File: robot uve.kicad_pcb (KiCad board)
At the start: 2 copper layers, 100 x 100 mm, 63 parts, among them J1 pulsador1, J10 HC-SR04, J11 HC-SR04, J12 HC-SR04, J13 NC - C - NA, J14 I2C_B, J15 I2C_C, J16 NeoPixel, J17 neopixel, J18 +5V IN, J19 GND, J2 I2C_A, J20 pulsador2, J21 IR, J22 pulsador2, J3 NC - C - NA, J4 comunicacion a rpi, J5 12V IN, J6 GND, J7 HC-SR04, J8 HC-SR04, J9 HC-SR04, K1 RELAY_C, K3 RELAY_C, P1 Digital, P10 CONN_01X01, P11 CONN_01X01, P12 CONN_01X01, P13 CONN_01X01, P14 motor3, P15 motor2, P16 Sensores de Linea, P17 motor1, P18 motor4, P2 Power, P3 Analog, P4 Analog, P5 PWM, P6 PWM, P7 Communication, P8 CONN_01X01, P9 CONN_01X01, Q1 2N7002, Q3 2N7002, Q4 2N7002, SW1 RST

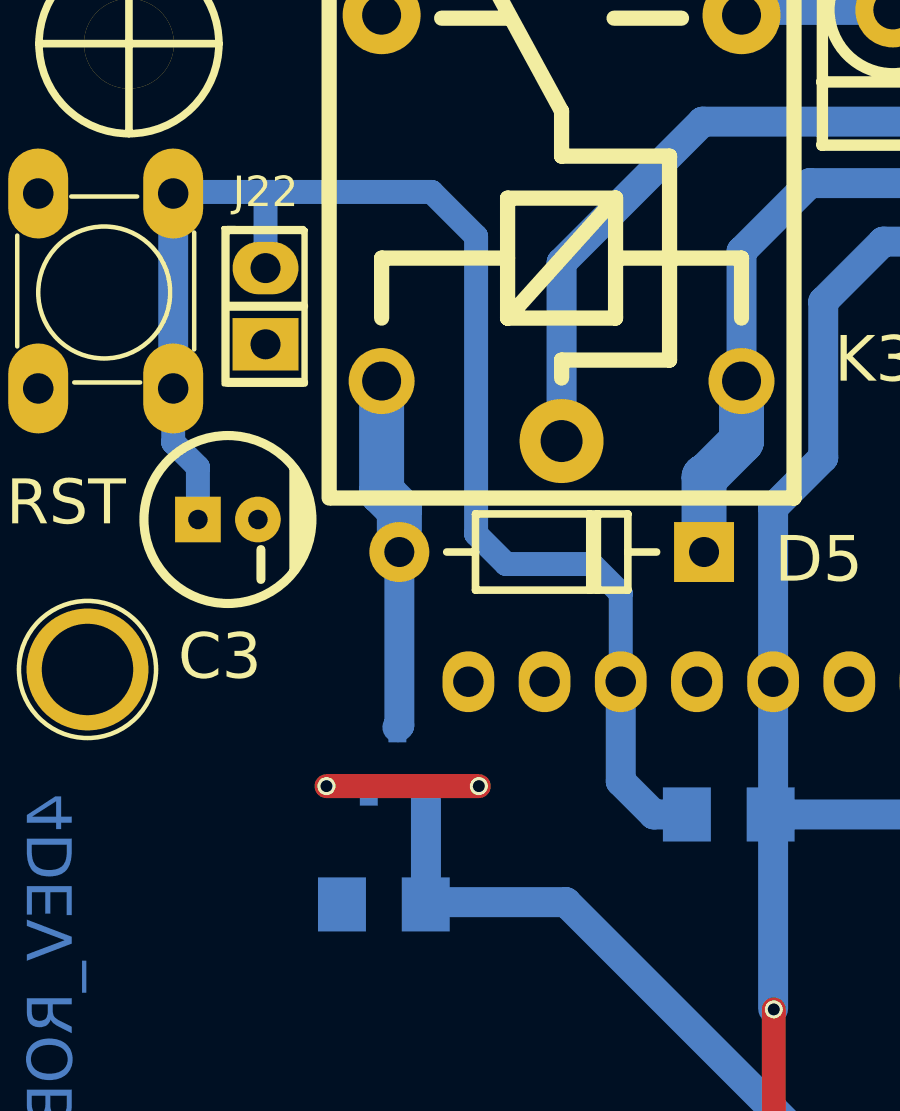
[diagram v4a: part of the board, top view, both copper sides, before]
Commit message: Img Pinout + avances en pcb
Agregue la imagen del pinout del arduino Mega en el sch, esta en una escala muy baja para que no moleste, en caso de necesitar revisar algo, cambiar la escala y luego volverla a la actual.
Cambie el icono del rotulo de SCH.
Movi un SOT-23 para que el poligono de GND pueda pasar por debajo del relay y evitar un jumper.
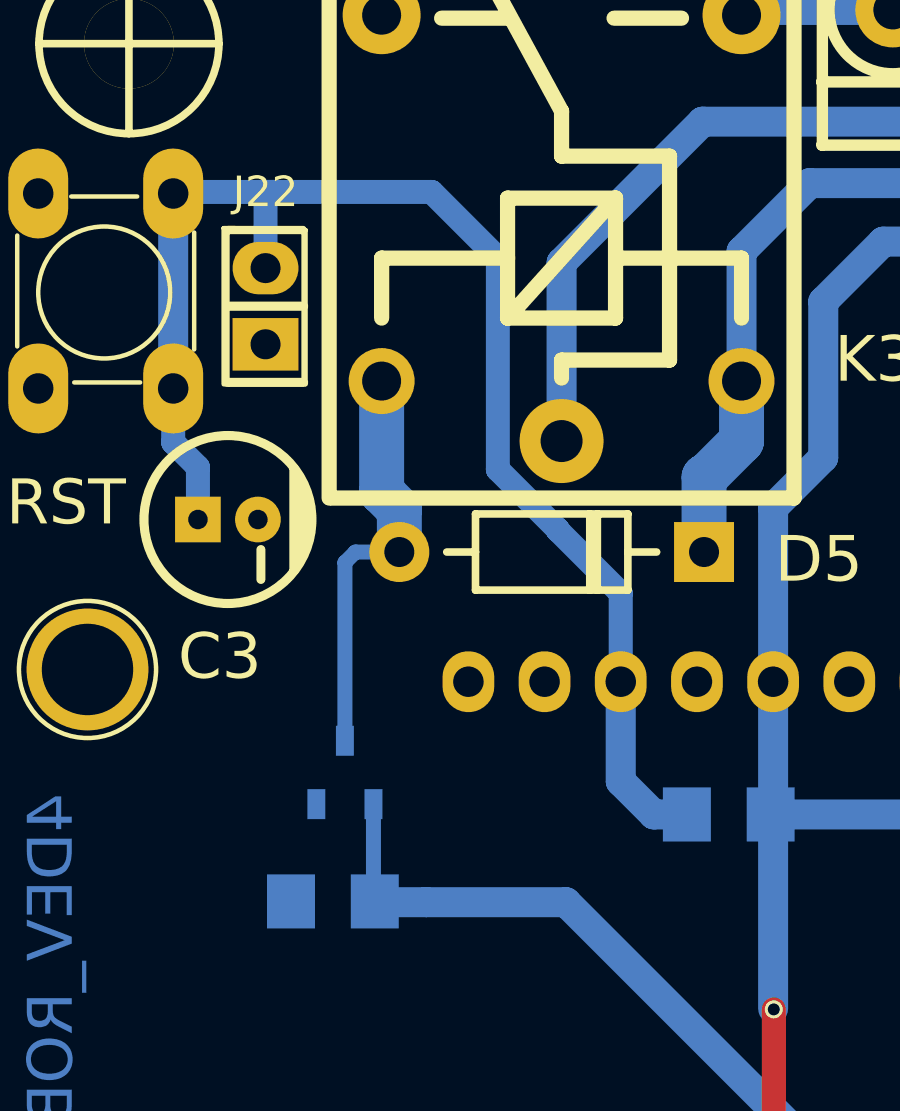
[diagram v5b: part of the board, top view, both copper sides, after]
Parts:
- moved Q4 1.81 mm to (117.2, 79.3)
- moved R5 1.70 mm to (116.8, 83.6)
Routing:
- net GND: track 64.3 -> 59.2 mm, vias 26 -> 24
- net Net-(D5-Pad1): track 11.8 -> 13.8 mm
- net /Reset: track 49.9 -> 48.2 mm
- net /3(**): track 59.5 -> 60.8 mm

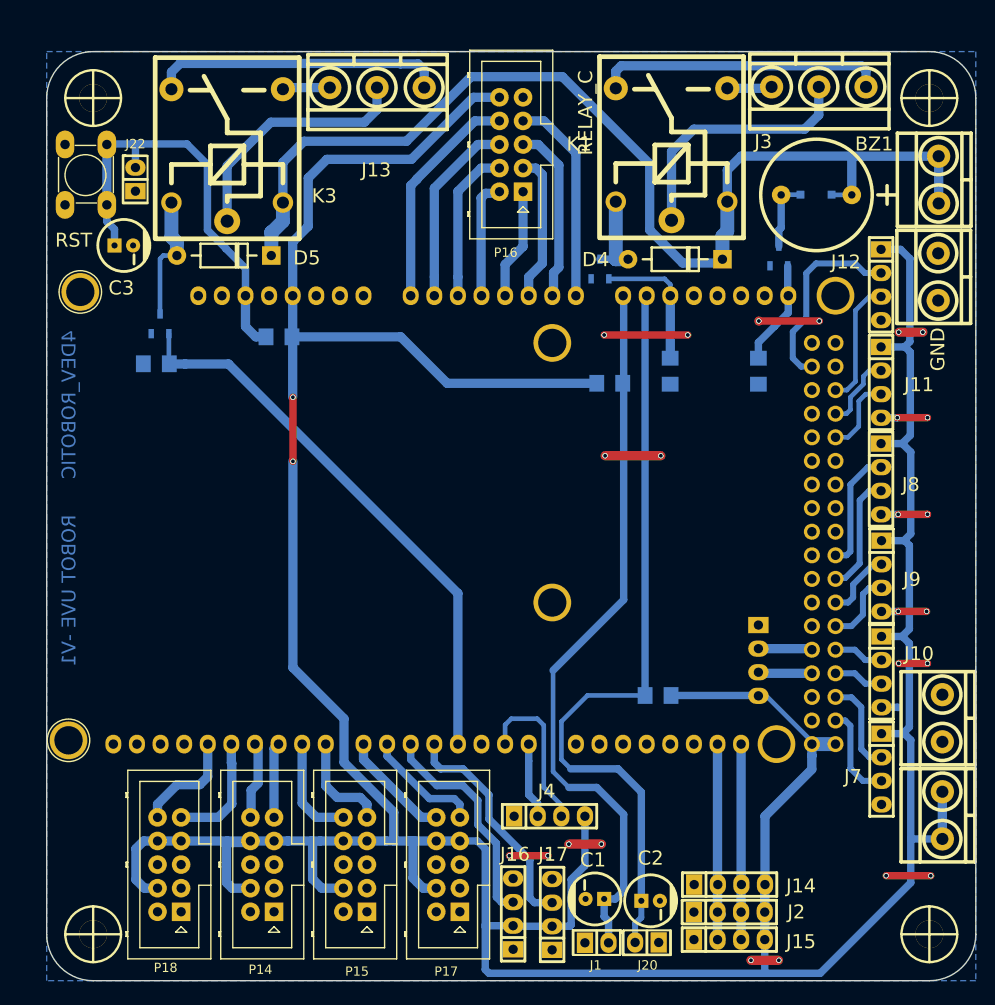
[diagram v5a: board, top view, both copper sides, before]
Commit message: MODIFICACIONES
se modifico pcb
se movio los conectores para eviar 2 vias mas
se cambio de huella pin_strip_4 a JST_4
al conectior de comunicacion a rpi
se esta armando la lista de componentes
se modifico el SCH para que reorganizar el ruteo del pcb
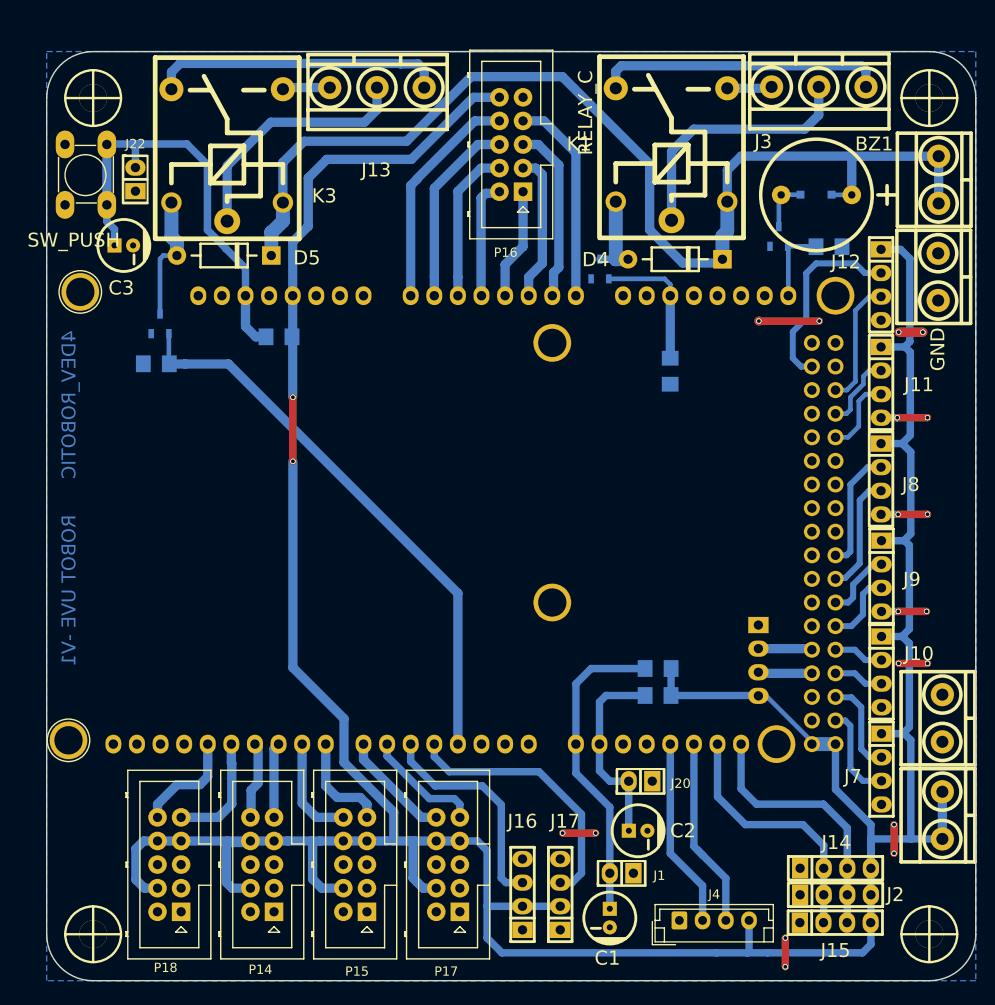
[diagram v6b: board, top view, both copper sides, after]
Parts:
- J22: value pulsador2 -> RST
- J4: footprint EESTN5:pin_strip_4 -> Connector_JST:JST_EH_B4B-EH-A_1x04_P2.50mm_Vertical
- SW1: value RST -> SW_PUSH
- moved R1 31.1 mm to (170.8, 116.4), turned to 0 degrees
- moved J4 17.9 mm to (173.1, 143.5)
- moved J20 17.4 mm to (168.9, 128.8)
- moved R2 15.4 mm to (189.2, 71.0), turned to 180 degrees
- moved J2 11.6 mm to (189.9, 140.8)
- moved J15 11.5 mm to (189.9, 143.8)
- moved J14 11.5 mm to (189.9, 137.9)
- moved C2 7.66 mm to (168.7, 133.9)
- moved J1 7.36 mm to (166.9, 138.7), turned to 180 degrees
- moved C1 2.61 mm to (165.6, 143.3), turned to 180 degrees
- moved J16 2.32 mm to (156.2, 140.7)
- moved J17 2.32 mm to (160.3, 140.7)
- moved Q1 2.10 mm to (183.8, 69.9)
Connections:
- C1 pad 1: /A8 -> /14(Tx3)
- C2 pad 1: /A9 -> /15(Rx3)
- J1 pad 2: /A8 -> /14(Tx3)
- J20 pad 2: /A9 -> /15(Rx3)
- J4 pad 2: /0(Rx0) -> /18(Tx1)
- J4 pad 3: /1(Tx0) -> /19(Rx1)
- P1 pad 11: (no net) -> /44
- P1 pad 12: (no net) -> /45
- P1 pad 13: (no net) -> /42
- P1 pad 14: (no net) -> /43
- P1 pad 15: (no net) -> /40
- P1 pad 16: (no net) -> /41
- P1 pad 17: (no net) -> /38
- P1 pad 18: (no net) -> /39
- P1 pad 19: (no net) -> /36
- P1 pad 21: (no net) -> /34
- P1 pad 23: (no net) -> /32
- P1 pad 25: (no net) -> /30
- P1 pad 31: (no net) -> /24
- P1 pad 33: (no net) -> /22
- P1 pad 4: (no net) -> /53(SS)
- P1 pad 5: (no net) -> /50(MISO)
- P1 pad 7: (no net) -> /48
- P1 pad 9: (no net) -> /46
- P10 pad 1: (no net) -> Net-(P10-Pad1)
- P11 pad 1: (no net) -> Net-(P11-Pad1)
- P12 pad 1: (no net) -> Net-(P12-Pad1)
- P13 pad 1: (no net) -> Net-(P13-Pad1)
- P14 pad 1: (no net) -> Net-(P14-Pad1)
- P14 pad 2: (no net) -> Net-(P14-Pad2)
- P14 pad 5: (no net) -> Net-(P14-Pad5)
- P14 pad 6: (no net) -> Net-(P14-Pad6)
- P15 pad 1: (no net) -> Net-(P15-Pad1)
- P15 pad 2: (no net) -> Net-(P15-Pad2)
- P15 pad 5: (no net) -> Net-(P15-Pad5)
- P15 pad 6: (no net) -> Net-(P15-Pad6)
- P17 pad 1: (no net) -> Net-(P17-Pad1)
- P17 pad 2: (no net) -> Net-(P17-Pad2)
- P17 pad 5: (no net) -> Net-(P17-Pad5)
- P17 pad 6: (no net) -> Net-(P17-Pad6)
- P18 pad 1: (no net) -> Net-(P18-Pad1)
- P18 pad 2: (no net) -> Net-(P18-Pad2)
- P18 pad 5: (no net) -> Net-(P18-Pad5)
- P18 pad 6: (no net) -> Net-(P18-Pad6)
- P2 pad 1: (no net) -> Net-(P2-Pad1)
- P2 pad 2: (no net) -> /IOREF
- P2 pad 4: (no net) -> +3V3
- P2 pad 8: (no net) -> /Vin
- P4 pad 4: (no net) -> /A11
- P4 pad 5: (no net) -> /A12
- P4 pad 6: (no net) -> /A13
- P4 pad 7: (no net) -> /A14
- P5 pad 1: (no net) -> /SCL
- P5 pad 2: (no net) -> /SDA
- P5 pad 3: (no net) -> /AREF
- P6 pad 6: (no net) -> /2(**)
- P7 pad 1: (no net) -> /14(Tx3)
- P7 pad 2: (no net) -> /15(Rx3)
- P7 pad 3: (no net) -> /16(Tx2)
- P7 pad 4: (no net) -> /17(Rx2)
- P7 pad 5: (no net) -> /18(Tx1)
- P7 pad 6: (no net) -> /19(Rx1)
- P8 pad 1: (no net) -> Net-(P8-Pad1)
- P9 pad 1: (no net) -> Net-(P9-Pad1)
- R1 pad 2: /A8 -> /14(Tx3)
- R3 pad 2: /A9 -> /15(Rx3)
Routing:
- net /A9: track 84.5 -> 0.11 mm
- net /A8: track 79.5 -> 0.00 mm
- net +5V: track 431.0 -> 376.6 mm
- net /14(Tx3): track 0.00 -> 33.9 mm
- net GND: track 59.2 -> 36.8 mm, vias 24 -> 18
- net /15(Rx3): track 0.00 -> 21.6 mm
- net /19(Rx1): track 0.00 -> 21.3 mm
- net /18(Tx1): track 0.00 -> 20.4 mm
- net /1(Tx0): track 17.6 -> 0.00 mm
- net /0(Rx0): track 8.17 -> 0.00 mm
- net /21(SCL): track 21.0 -> 28.2 mm
- net /20(SDA): track 21.2 -> 27.8 mm
- net /4(**): track 24.8 -> 28.8 mm
- net /A15: track 11.3 -> 8.41 mm
- net Net-(BZ1-Pad2): track 8.06 -> 5.61 mm

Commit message: Reasignación de pines y layout
Cambié la conexion del control IR, de la comunicacion serie hacia la RPI.
Cambié el footprint de los capacitores de los pulsadores y redibuje el pcb para contemplar los cambios
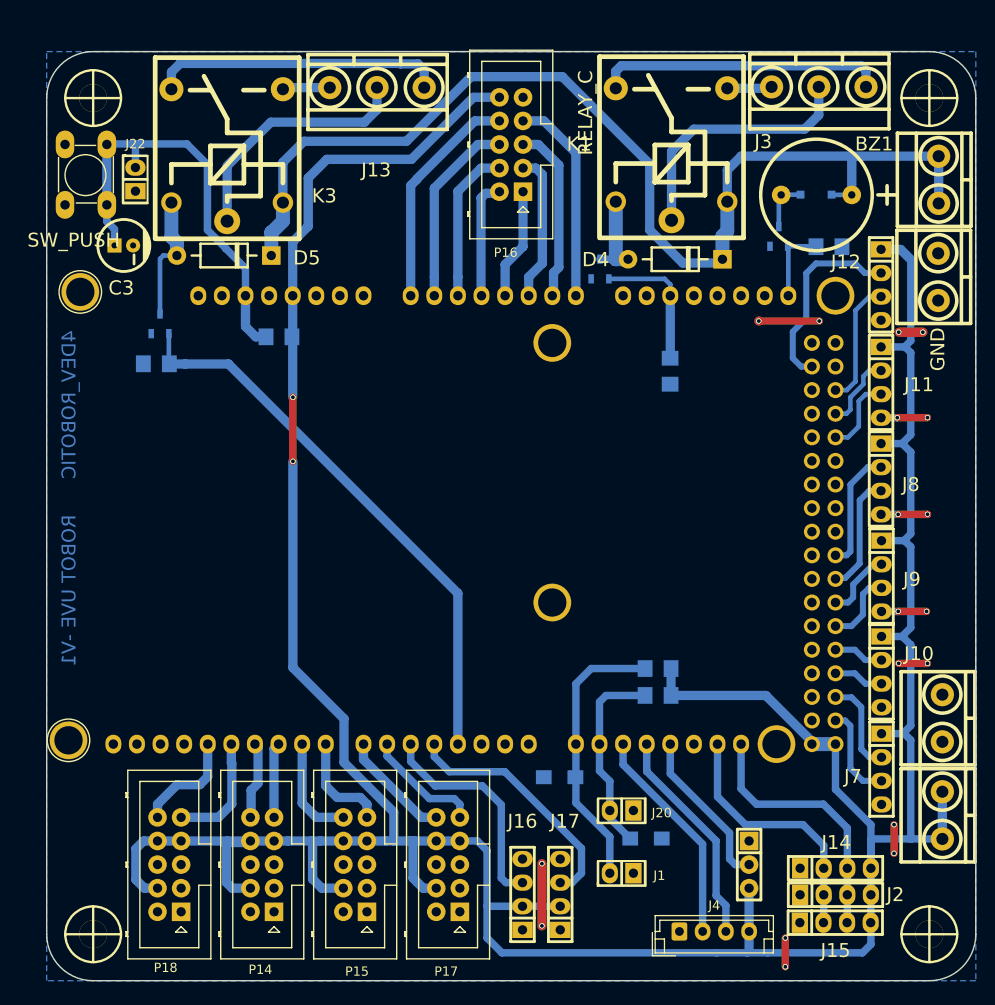
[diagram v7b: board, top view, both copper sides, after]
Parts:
- C1, C2: footprint EESTN5:CAP_ELEC_5x11mm -> EESTN5:CAP_TAN_A; moved to B.Cu
- J21: footprint EESTN5:pin_strip_4 -> EESTN5:Pin_Strip_3; moved to F.Cu
- moved J21 22.0 mm to (180.6, 137.5)
- moved C1 16.1 mm to (160.2, 128.1)
- moved J20 3.76 mm to (166.9, 132.0)
- moved C2 1.19 mm to (169.5, 134.7), turned to 0 degrees
- moved J4 1.19 mm to (173.1, 144.7)
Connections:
- J21 pad 2: /28 -> /18(Tx1)
- J21 pad 3: /26 -> +5V
- J4 pad 2: /18(Tx1) -> /16(Tx2)
- J4 pad 3: /19(Rx1) -> /17(Rx2)
- P1 pad 11: /44 -> (no net)
- P1 pad 12: /45 -> (no net)
- P1 pad 13: /42 -> (no net)
- P1 pad 14: /43 -> (no net)
- P1 pad 15: /40 -> (no net)
- P1 pad 16: /41 -> (no net)
- P1 pad 17: /38 -> (no net)
- P1 pad 18: /39 -> (no net)
- P1 pad 19: /36 -> (no net)
- P1 pad 21: /34 -> (no net)
- P1 pad 23: /32 -> (no net)
- P1 pad 25: /30 -> (no net)
- P1 pad 27: /28 -> (no net)
- P1 pad 29: /26 -> (no net)
- P1 pad 31: /24 -> (no net)
- P1 pad 33: /22 -> (no net)
- P1 pad 4: /53(SS) -> (no net)
- P1 pad 5: /50(MISO) -> (no net)
- P1 pad 7: /48 -> (no net)
- P1 pad 9: /46 -> (no net)
- P10 pad 1: Net-(P10-Pad1) -> (no net)
- P11 pad 1: Net-(P11-Pad1) -> (no net)
- P12 pad 1: Net-(P12-Pad1) -> (no net)
- P13 pad 1: Net-(P13-Pad1) -> (no net)
- P14 pad 1: Net-(P14-Pad1) -> (no net)
- P14 pad 2: Net-(P14-Pad2) -> (no net)
- P14 pad 5: Net-(P14-Pad5) -> (no net)
- P14 pad 6: Net-(P14-Pad6) -> (no net)
- P15 pad 1: Net-(P15-Pad1) -> (no net)
- P15 pad 2: Net-(P15-Pad2) -> (no net)
- P15 pad 5: Net-(P15-Pad5) -> (no net)
- P15 pad 6: Net-(P15-Pad6) -> (no net)
- P17 pad 1: Net-(P17-Pad1) -> (no net)
- P17 pad 2: Net-(P17-Pad2) -> (no net)
- P17 pad 5: Net-(P17-Pad5) -> (no net)
- P17 pad 6: Net-(P17-Pad6) -> (no net)
- P18 pad 1: Net-(P18-Pad1) -> (no net)
- P18 pad 2: Net-(P18-Pad2) -> (no net)
- P18 pad 5: Net-(P18-Pad5) -> (no net)
- P18 pad 6: Net-(P18-Pad6) -> (no net)
- P2 pad 1: Net-(P2-Pad1) -> (no net)
- P2 pad 2: /IOREF -> (no net)
- P2 pad 4: +3V3 -> (no net)
- P2 pad 8: /Vin -> (no net)
- P4 pad 1: /A8 -> (no net)
- P4 pad 2: /A9 -> (no net)
- P4 pad 4: /A11 -> (no net)
- P4 pad 5: /A12 -> (no net)
- P4 pad 6: /A13 -> (no net)
- P4 pad 7: /A14 -> (no net)
- P5 pad 1: /SCL -> (no net)
- P5 pad 2: /SDA -> (no net)
- P5 pad 3: /AREF -> (no net)
- P6 pad 6: /2(**) -> (no net)
- P6 pad 7: /1(Tx0) -> (no net)
- P6 pad 8: /0(Rx0) -> (no net)
- P7 pad 6: /19(Rx1) -> (no net)
- P8 pad 1: Net-(P8-Pad1) -> (no net)
- P9 pad 1: Net-(P9-Pad1) -> (no net)
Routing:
- net /16(Tx2): track 0.00 -> 23.7 mm
- net /17(Rx2): track 0.00 -> 23.7 mm
- net /19(Rx1): track 21.3 -> 0.00 mm
- net /26: track 5.81 -> 0.00 mm
- net /28: track 5.81 -> 0.00 mm
- net +5V: track 376.6 -> 381.1 mm
- net /14(Tx3): track 33.9 -> 30.0 mm
- net GND: track 36.8 -> 39.9 mm
- net /18(Tx1): track 20.4 -> 17.4 mm
- net /4(**): track 28.8 -> 26.7 mm

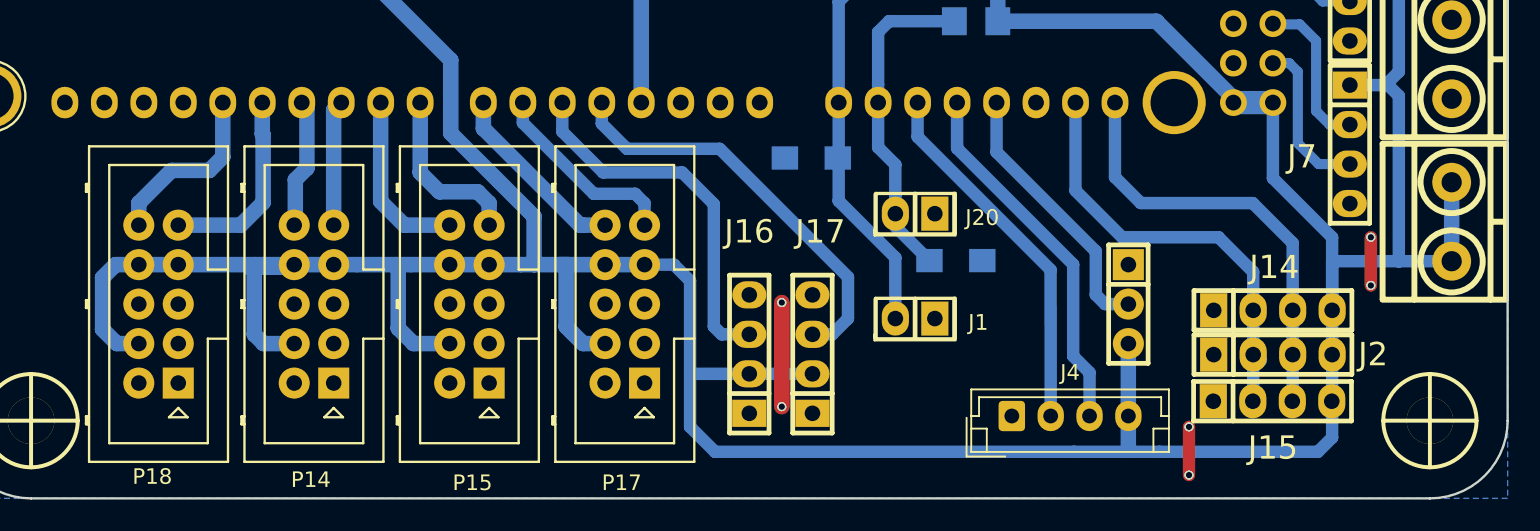
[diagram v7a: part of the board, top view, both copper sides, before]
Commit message: VCC width
Cambié el ancho de la pista de alimentación
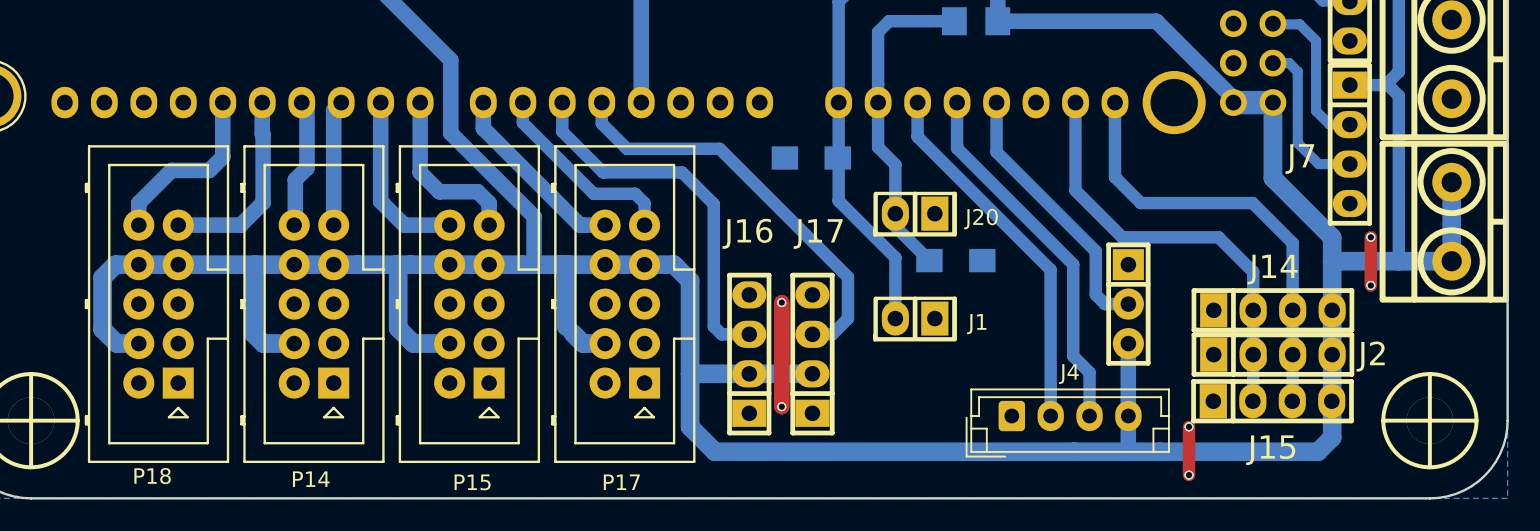
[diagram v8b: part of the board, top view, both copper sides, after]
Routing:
- net +5V: track 381.1 -> 378.1 mm
